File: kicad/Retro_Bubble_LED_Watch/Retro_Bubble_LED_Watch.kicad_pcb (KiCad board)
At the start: 2 copper layers, 36 x 36 mm, 32 parts, among them J2 AVR ISP Connector, Q1 BSS138, Q2 BSS138, Q3 BSS138, Q4 BSS138, SW1 MODE, SW2 UP, U2 ATmega328PB-A, U3 DS1337S+

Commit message: first partial layout
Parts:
- added G***: LOGO, LOGO, F.Cu at (264.5, 65.5)
- moved R6 3.25 mm to (245.5, 97.8), turned to -90 degrees
- moved R7 3.25 mm to (245.5, 94.5)
- moved R10 2.14 mm to (246.2, 100.2), turned to 180 degrees
- moved SW2 1.00 mm to (241.5, 94.5)
- moved J2 0.35 mm to (272.0, 92.3)
- moved SW1 0.25 mm to (271.2, 82.0)
- turned BT1 to 90 degrees
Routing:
- net Net-(DS1-DP): track 0.00 -> 29.8 mm, vias 0 -> 2
- net +BATT: track 7.88 -> 28.9 mm, vias 0 -> 1
- net Net-(U2-PD0): track 1.68 -> 21.8 mm, vias 1 -> 2
- net Net-(DS1-e): track 0.00 -> 13.5 mm
- net Net-(U2-PD5): track 3.24 -> 14.5 mm
- net Net-(U2-PD4): track 0.00 -> 8.65 mm
- net Net-(U2-PD7): track 1.88 -> 10.2 mm, vias 1 -> 2
- net Net-(U2-PD1): track 1.60 -> 9.67 mm, vias 1 -> 2
- net Net-(DS1-c): track 0.00 -> 7.92 mm
- net Net-(U2-PD3): track 0.00 -> 5.34 mm
- net Net-(DS1-CA2): track 2.05 -> 7.09 mm, vias 1 -> 2
- net Net-(DS1-CA5): track 0.00 -> 4.56 mm, vias 0 -> 2
- net Net-(DS1-CA4): track 0.00 -> 4.49 mm, vias 0 -> 2
- net Net-(U2-PD2): track 0.00 -> 3.50 mm
- net Net-(U2-PD6): track 2.90 -> 6.30 mm
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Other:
- outline, holes or cut-outs redrawn

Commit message: new layout
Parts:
- removed BZ1: Buzzer, Buzzer_Beeper:Buzzer_Murata_PKLCS1212E
- removed Q1, Q2, Q3, Q4: BSS138, Package_TO_SOT_SMD:SOT-23
- removed R14, R15, R16, R17, R18, R19, R20, R21: 10k, Resistor_SMD:R_0603_1608Metric
- added R11: 10k, Resistor_SMD:R_0603_1608Metric, F.Cu at (207.0, 99.8)
- J2: footprint Connector_PinHeader_2.54mm:PinHeader_2x03_P2.54mm_Vertical -> Connector_PinHeader_2.54mm:PinHeader_2x03_P2.54mm_Vertical_SMD
- XTAL1: moved to F.Cu
- moved J2 90.4 mm to (181.8, 87.0), turned to -90 degrees
- moved G*** 63.8 mm to (202.2, 79.5)
- moved XTAL1 61.2 mm to (208.5, 77.8), turned to 180 degrees
- moved R9 59.5 mm to (204.0, 91.2)
- moved R8 54.3 mm to (204.0, 89.8)
- moved U3 52.5 mm to (217.0, 78.8), turned to 0 degrees
- moved R4 49.1 mm to (204.0, 88.2)
- moved SW1 45.8 mm to (225.8, 76.8), turned to 135 degrees
- moved R3 43.7 mm to (204.0, 86.8)
- moved DS1 41.8 mm to (214.8, 88.0)
- moved C1 39.8 mm to (208.5, 99.8), turned to -90 degrees
- moved U2 39.8 mm to (214.8, 99.8), turned to 180 degrees
- moved BT1 39.3 mm to (214.7, 88.0), turned to 180 degrees
- moved R2 38.8 mm to (226.5, 81.0), turned to 180 degrees
- moved R1 37.4 mm to (225.5, 84.0), turned to 180 degrees
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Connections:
- J2 pad 1: /HI_MISO -> /MISO
- J2 pad 2: +5V -> +BATT
- J2 pad 3: /HI_SCK -> /SCK
- J2 pad 4: /HI_MOSI -> /MOSI
- J2 pad 5: /~{HI_RESET} -> /~{RESET}
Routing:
- net /UP_BUTTON: track 2.50 -> 59.1 mm, vias 1 -> 2
- net /MODE_BUTTON: track 2.08 -> 50.4 mm, vias 1 -> 2
- net /~{INTA}: track 14.7 -> 50.6 mm
- net +BATT: track 28.9 -> 60.1 mm, vias 1 -> 3
- net /SDA: track 12.8 -> 40.8 mm, vias 0 -> 2
- net /SCL: track 15.7 -> 38.8 mm
- net Net-(DS1-DP): track 29.8 -> 9.66 mm, vias 2 -> 0
- net Net-(DS1-g): track 3.52 -> 22.7 mm
- net Net-(U2-PD2): track 3.50 -> 22.3 mm, vias 0 -> 2
- net Net-(U2-PD0): track 21.8 -> 5.29 mm, vias 2 -> 1
- net Net-(DS1-CA1): track 6.57 -> 21.0 mm
- net Net-(U2-PD4): track 8.65 -> 21.8 mm, vias 0 -> 2
- net Net-(DS1-f): track 3.49 -> 16.4 mm
- net Net-(DS1-CA4): track 4.49 -> 17.3 mm
- net Net-(DS1-CA2): track 7.09 -> 18.6 mm
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- added copper zone on B.Cu, net GND
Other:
- board size 36 x 36 mm -> 35 x 35 mm
- board text added: "Rev. 1.0"
- board text added: "Szymon Bartosik 2024"

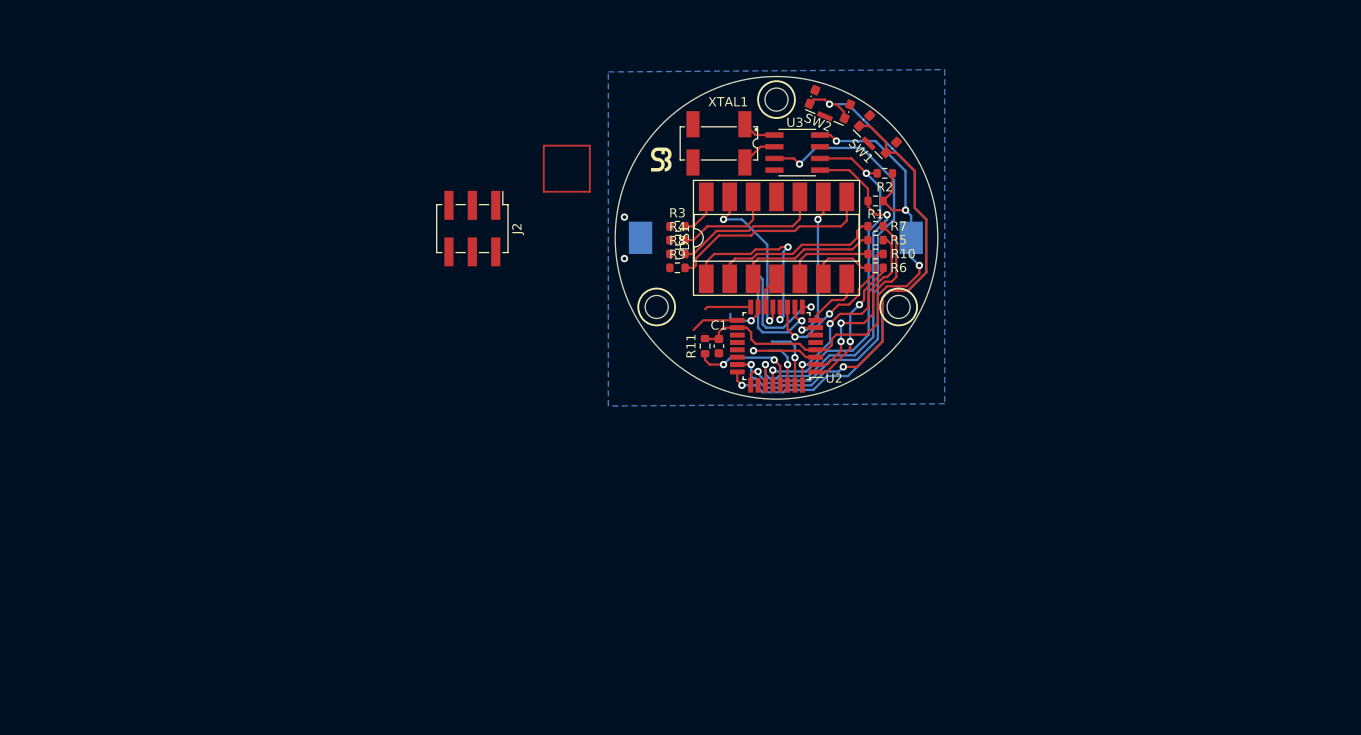
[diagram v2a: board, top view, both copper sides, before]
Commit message: added socket and display models
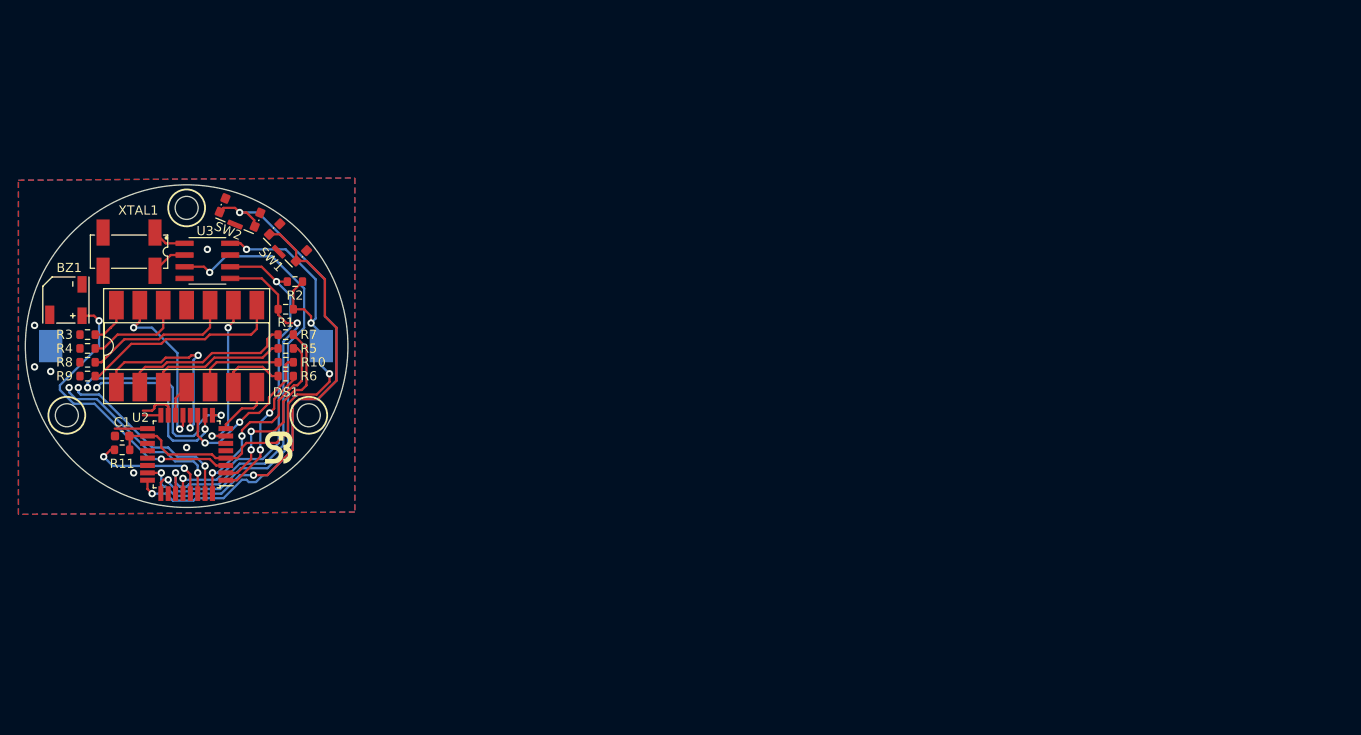
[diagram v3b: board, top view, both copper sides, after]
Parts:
- removed J2: AVR ISP Connector, Connector_PinHeader_2.54mm:PinHeader_2x03_P2.54mm_Vertical_SMD
- added BZ1: Buzzer, footprints:FUET-5020, F.Cu at (141.5, 94.8)
- moved C1 65.5 mm to (143.8, 109.5), turned to 180 degrees
- moved BT1 65.1 mm to (150.7, 99.8)
- moved DS1 65.1 mm to (150.8, 99.8)
- moved R1 65.1 mm to (161.5, 95.8)
- moved R10 65.1 mm to (161.5, 101.5)
- moved R2 65.1 mm to (162.5, 92.8)
- moved R3 65.1 mm to (140.0, 98.5)
- moved R4 65.1 mm to (140.0, 100.0)
- moved R5 65.1 mm to (161.5, 100.0)
- moved R6 65.1 mm to (161.5, 103.0)
- moved R7 65.1 mm to (161.5, 98.5)
- moved R8 65.1 mm to (140.0, 101.5)
- moved R9 65.1 mm to (140.0, 103.0)
- moved SW1 65.1 mm to (161.8, 88.5)
- moved SW2 65.1 mm to (156.5, 85.2)
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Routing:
- net Net-(BZ1-+): track 7.04 -> 32.7 mm, vias 1 -> 2
- net Net-(U2-PD0): track 5.29 -> 20.8 mm, vias 1 -> 2
- net Net-(U2-PD1): track 6.94 -> 20.6 mm, vias 1 -> 2
- net Net-(U2-PD5): track 13.2 -> 23.0 mm, vias 1 -> 2
- net Net-(U2-PD6): track 13.2 -> 19.7 mm, vias 1 -> 2
- net /MISO: track 5.05 -> 1.95 mm
- net /~{RESET}: track 11.8 -> 13.8 mm
- net /SCK: track 5.03 -> 3.55 mm
- net /MOSI: track 4.66 -> 4.21 mm, vias 1 -> 0
- net GND: vias 2 -> 6
- added copper zone on F.Cu, net GND

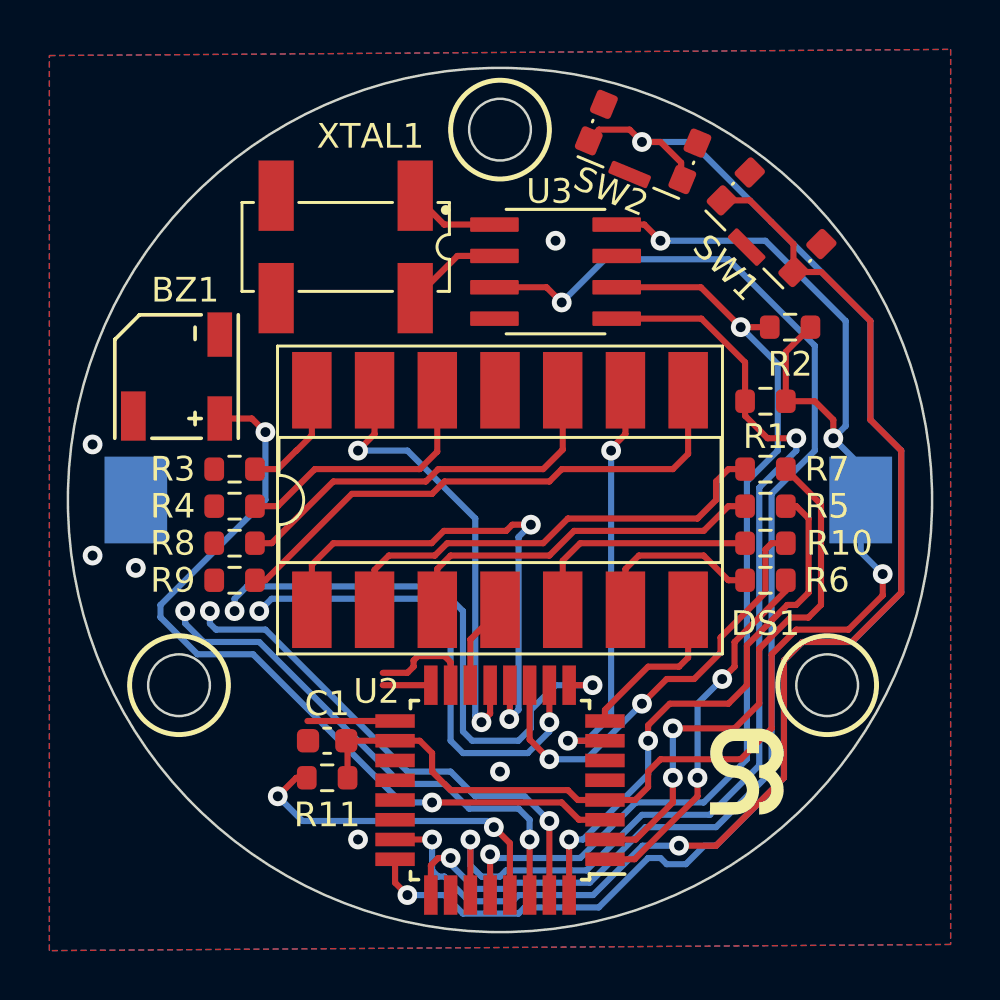
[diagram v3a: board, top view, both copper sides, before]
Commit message: final PCB design + gerber + initial models
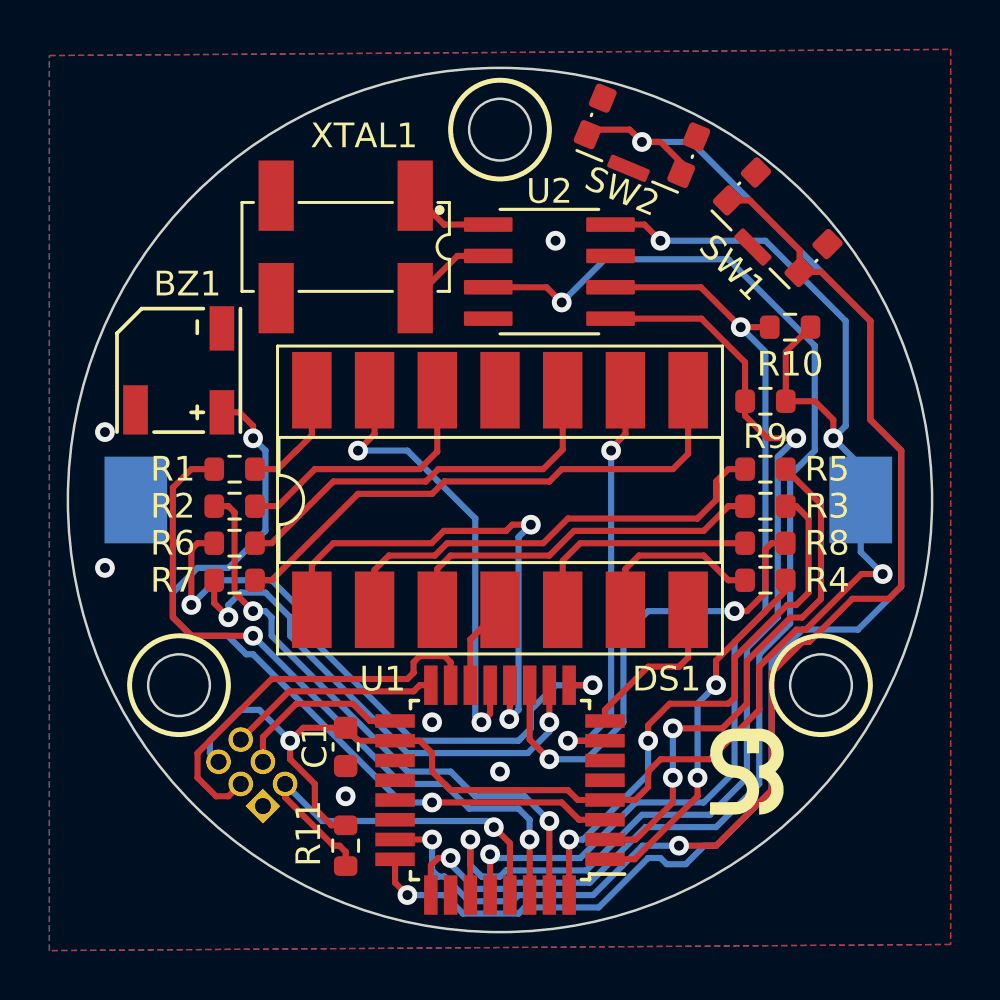
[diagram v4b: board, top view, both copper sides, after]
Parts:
- added J1: ISP Programming Connector, Connector_PinHeader_1.27mm:PinHeader_2x03_P1.27mm_Vertical, B.Cu at (141.1, 112.1)
- BZ1: value Buzzer -> FUET-5020
- R1: renamed from R3; value 680R -> 360R
- R2: renamed from R4; value 680R -> 360R
- R3: renamed from R5; value 680R -> 360R
- R4: renamed from R6; value 680R -> 360R
- R5: renamed from R7; value 680R -> 360R
- R6: renamed from R8; value 680R -> 360R
- R7: renamed from R9; value 680R -> 360R
- R8: renamed from R10; value 680R -> 360R
- SW1: value MODE -> KMS231G
- SW2: value UP -> KMS231G
- moved R11 2.85 mm to (144.5, 113.8), turned to -90 degrees
- moved C1 0.79 mm to (144.5, 109.8), turned to -90 degrees
- moved BZ1 0.26 mm to (141.6, 94.5)
- moved SW2 0.25 mm to (156.5, 85.0)
- moved SW1 0.25 mm to (162.0, 88.5)
- moved U2 0.25 mm to (152.8, 90.5)
- renumbered R2 to R10, R1 to R9, U2 to U1, U3 to U2
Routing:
- net /MOSI: track 4.21 -> 16.4 mm
- net +BATT: track 59.7 -> 69.9 mm, vias 3 -> 4
- net Net-(U1-PD0): track 20.8 -> 28.1 mm
- net /MISO: track 1.95 -> 8.61 mm
- net /SCK: track 3.55 -> 7.20 mm
- net Net-(U1-PD1): track 20.6 -> 24.2 mm
- net /~{RESET}: track 13.8 -> 16.7 mm, vias 2 -> 1
- net Net-(U1-PD5): track 23.0 -> 25.4 mm
- net Net-(U1-PD7): track 17.9 -> 19.6 mm
- net Net-(U1-PD6): track 19.7 -> 20.8 mm
- net /SDA: track 41.0 -> 41.7 mm
- net /~{INTA}: track 50.6 -> 51.4 mm
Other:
- outline, holes or cut-outs redrawn

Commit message: finished rev. 1.0
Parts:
- R1, R2, R3, R4, R5, R6, R7, R8: value 360R -> 680R
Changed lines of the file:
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@@
         (effects (font (size 1 1) (thickness 0.15)))
     )
-    (fp_text value "360R" (at 0 1.43) (layer "F.Fab")
+    (fp_text value "680R" (at 0 1.43) (layer "F.Fab")
         (effects (font (size 1 1) (thickness 0.15)))
     )
@@
         (effects (font (size 1 1) (thickness 0.15)))
     )
-    (fp_text value "360R" (at 0 1.43) (layer "F.Fab")
+    (fp_text value "680R" (at 0 1.43) (layer "F.Fab")
         (effects (font (size 1 1) (thickness 0.15)))
     )
@@
         (effects (font (size 1 1) (thickness 0.15)))
     )
-    (fp_text value "360R" (at 0 1.43) (layer "F.Fab")
+    (fp_text value "680R" (at 0 1.43) (layer "F.Fab")
         (effects (font (size 1 1) (thickness 0.15)))
     )
@@
         (effects (font (size 1 1) (thickness 0.15)))
     )
-    (fp_text value "360R" (at 0 1.43) (layer "F.Fab")
+    (fp_text value "680R" (at 0 1.43) (layer "F.Fab")
         (effects (font (size 1 1) (thickness 0.15)))
     )
@@
         (effects (font (size 1 1) (thickness 0.15)))
     )
-    (fp_text value "360R" (at 0 1.43) (layer "F.Fab")
+    (fp_text value "680R" (at 0 1.43) (layer "F.Fab")
         (effects (font (size 1 1) (thickness 0.15)))
     )
@@
         (effects (font (size 1 1) (thickness 0.15)))
     )
-    (fp_text value "360R" (at 0 1.43) (layer "F.Fab")
+    (fp_text value "680R" (at 0 1.43) (layer "F.Fab")
         (effects (font (size 1 1) (thickness 0.15)))
     )
@@
         (effects (font (size 1 1) (thickness 0.15)))
     )
-    (fp_text value "360R" (at 0 1.43) (layer "F.Fab")
+    (fp_text value "680R" (at 0 1.43) (layer "F.Fab")
         (effects (font (size 1 1) (thickness 0.15)))
     )
@@
         (effects (font (size 1 1) (thickness 0.15)))
     )
-    (fp_text value "360R" (at 0 1.43) (layer "F.Fab")
-        (effects (font (size 1 1) (thickness 0.15)))
-    )
+    (fp_text value "680R" (at 0 1.43) (layer "F.Fab")
+        (effects (font (size 1 1) (thickness 0.15)))
+    )

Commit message: Rev. 1.1
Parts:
- removed BZ1: FUET-5020, footprints:FUET-5020
- added C2: 100n, Capacitor_SMD:C_0603_1608Metric, F.Cu at (143.8, 108.8)
- added C3: 100n, Capacitor_SMD:C_0603_1608Metric, F.Cu at (144.5, 111.0)
- added J2: Pad Connector, footprints:Pad_Conn_2x1_2x1mm_2.54mm, F.Cu at (140.0, 93.3)
- BT1: value Panasonic CR2032 -> Panasonic CR2032/BN; footprint Battery:BatteryHolder_Keystone_1058_1x2032 -> Battery:BatteryHolder_Keystone_1060_1x2032
- DS1: value 5082-7415 -> HP 5082-7415
- R1, R2, R3, R4, R5, R6, R7, R8: value 680R -> 330R
- XTAL1: footprint Crystal:Crystal_SMD_SeikoEpson_MC306-4Pin_8.0x3.2mm_HandSoldering -> footprints:LFXTAL016178Reel
- moved C1 12.8 mm to (157.2, 110.5), turned to 90 degrees
- moved XTAL1 5.14 mm to (144.5, 84.4)
- moved BT1 2.25 mm to (150.7, 97.5)
- moved R11 1.52 mm to (143.0, 113.5), turned to 180 degrees
- moved G*** 0.75 mm to (161.5, 110.7)
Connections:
- U1 pad 20: unconnected-(U1-AREF-Pad20) -> Net-(U1-AREF)
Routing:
- net Net-(J2-Pin_2): track 32.6 -> 38.5 mm
- net Net-(U1-AREF): track 0.00 -> 2.26 mm
- net /~{RESET}: track 16.7 -> 14.8 mm
- net /SCK: track 7.20 -> 8.82 mm
- net /MISO: track 8.61 -> 9.59 mm
- net /MODE_BUTTON: track 50.2 -> 49.3 mm
- net Net-(U2-X2): track 3.67 -> 4.49 mm
- net /UP_BUTTON: track 59.5 -> 58.9 mm
- net GND: vias 6 -> 16
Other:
- board text added: "Rev. 1.1"
- board text removed: "Rev. 1.0"
